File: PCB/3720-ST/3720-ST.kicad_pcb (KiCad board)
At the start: 2 copper layers, 150 x 110 mm, 34 parts, among them J1 1546216-8, J10 1546216-8, J11 1546216-8, J12 1546216-8, J13 1546216-8, J14 1546216-8, J15 1546216-8, J16 1546216-8, J2 1546216-8, J3 1546216-8, J4 1546216-8, J5 1546216-8, J6 1546216-8, J7 1546216-8, J8 1546216-8, J9 1546216-8, U1 TMP275AID, U2 TMP275AID

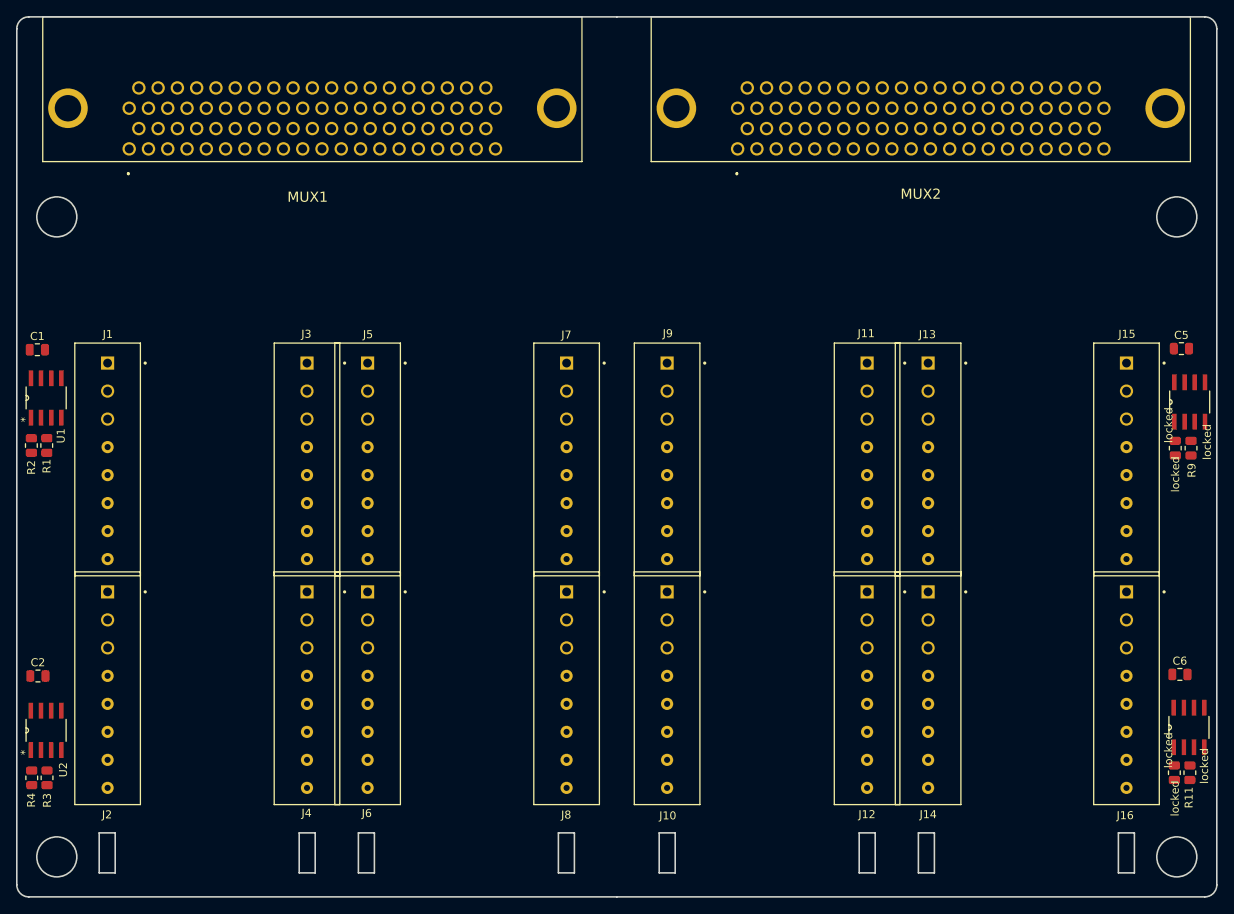
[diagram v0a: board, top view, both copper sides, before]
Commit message: final board layout before routing
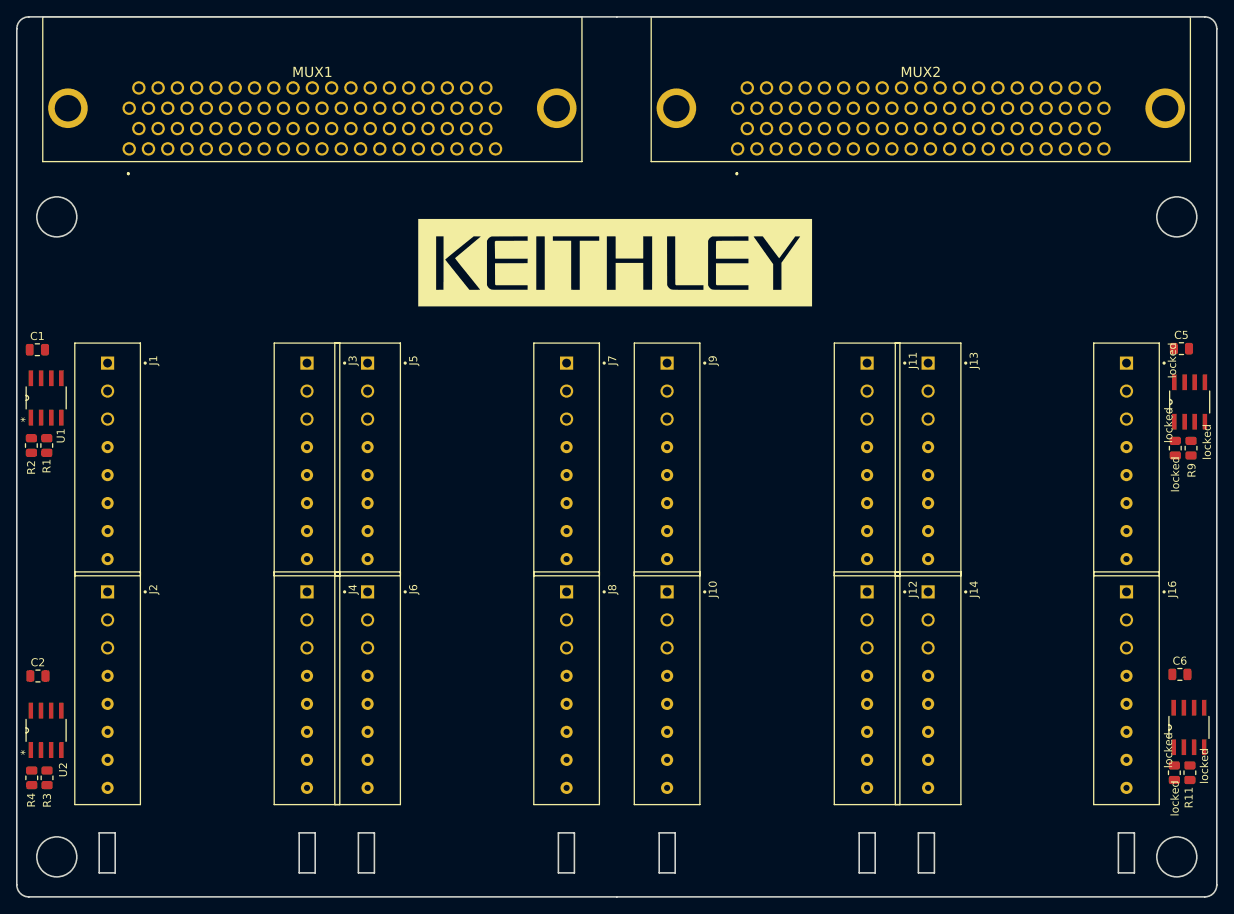
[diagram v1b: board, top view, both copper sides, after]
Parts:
- added G***: LOGO, BVKSound:Keithley_Logo, F.Cu at (99.8, 70.7)
- J1: value 1546216-8 -> locked
- renumbered J15 to locked
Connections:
- MUX1 pad 76: /+ILK -> /ILK1
- MUX1 pad 78: /-ILK -> /ILK1
- MUX2 pad 76: /+ILK -> /ILK2
- MUX2 pad 78: /-ILK -> /ILK2
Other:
- copper layers 2 -> 4

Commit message: Design finished, ready for review
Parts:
- added G***: LOGO, BVKSound:BVKSound_Logo, B.Cu at (156.8, 69.7)
- added QR*****: www.bvksound.be, BVKSound:www.bvksound.be, B.Cu at (138.0, 67.1)
- renumbered locked to J15
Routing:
- net SDA: track 0.00 -> 317.5 mm, vias 0 -> 4
- net +3V3: track 0.00 -> 299.9 mm, vias 0 -> 2
- net GND: track 0.00 -> 284.5 mm, vias 0 -> 153
- net SCL: track 0.00 -> 252.5 mm, vias 0 -> 3
- net /31H: track 0.00 -> 93.6 mm
- net /1H: track 0.00 -> 93.2 mm
- net /31L: track 0.00 -> 91.1 mm
- net /18H: track 0.00 -> 90.5 mm
- net /1L: track 0.00 -> 88.6 mm
- net /2H: track 0.00 -> 88.3 mm
- net /48H: track 0.00 -> 88.0 mm
- net /32H: track 0.00 -> 86.3 mm
- net /18L: track 0.00 -> 86.0 mm
- net /20H: track 0.00 -> 85.6 mm
- net /2L: track 0.00 -> 85.3 mm
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- added copper zone on B.Cu, net GND
- added copper zone on F.Cu, net GND
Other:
- copper layers 4 -> 6
- board text added: "Keithley 3720-ST BVKSound 2022-03"

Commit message: silkscreen added + fix in design
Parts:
- removed QR*****: www.bvksound.be, BVKSound:www.bvksound.be
- added QR1: www.bvksound.be, BVKSound:www.bvksound.be, B.Cu at (136.4, 67.2)
- moved G1 1.17 mm to (156.1, 68.7)
- renumbered G*** to G1
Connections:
- J1 pad 5: /11H -> /11L
- J1 pad 6: /11L -> /11H
- MUX2 pad 40: /39H -> /41H
- MUX2 pad 41: /41H -> /41L
- MUX2 pad 42: /41L -> /33H
- MUX2 pad 43: /33H -> /33L
- MUX2 pad 44: /33L -> /51H
- MUX2 pad 45: /51H -> /51L
- MUX2 pad 46: /51L -> /59H
- MUX2 pad 47: /59H -> /59L
- MUX2 pad 48: /59L -> /40H
- MUX2 pad 49: /40H -> /40L
- MUX2 pad 50: /40L -> /32H
- MUX2 pad 51: /32H -> /32L
- MUX2 pad 52: /32L -> /46L
- MUX2 pad 53: /46L -> unconnected-(MUX2-Pad53)
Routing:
- net GND: track 284.5 -> 114.8 mm, vias 153 -> 194
- net /11H: track 48.8 -> 52.3 mm
- net /11L: track 52.5 -> 49.0 mm
- net /45H: track 36.2 -> 33.9 mm
- net /51H: track 73.6 -> 75.5 mm
- net /51L: track 70.2 -> 71.7 mm
- net /36H: track 68.8 -> 67.4 mm
- net /41H: track 54.3 -> 53.0 mm
- net SCL: track 252.5 -> 253.7 mm
- net /34H: track 78.4 -> 77.3 mm
- net /33H: track 84.9 -> 83.8 mm
- net /43H: track 45.1 -> 44.0 mm
- net /57L: track 46.1 -> 45.0 mm
- net /41L: track 51.8 -> 50.8 mm
- net /32H: track 86.3 -> 87.3 mm
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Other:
- board text added: "15L 15H 13L 13H 11L 11H 9L 9H"
- board text added: "16L 16H 14L 14H 12L 12H 10L 10H"
- board text added: "23L 23H 21L 21H 19L 19H 17L 17H"
- board text added: "24L 24H 22L 22H 20L 20H 18L 18H"
- board text added: "37L 37H 35L 35H 33L 33H 31L 31H"
- board text added: "38L 38H 36L 36H 34L 34H 32L 32H"
- board text added: "45L 45H 43L 43H 41L 41H 39L 39H"
- board text added: "46L 46H 44L 44H 42L 42H 40L 40H"
- board text added: "53L 53H 51L 51H 49L 49H 47L 47H"
- board text added: "54L 54H 52L 52H 50L 50H 48L 48H"
- board text added: "7L 7H 5L 5H 3L 3H 1L 1H"
- board text added: "8L 8H 6L 6H 4L 4H 2L 2H"
- board text added: "MUX_1L MUX_1H 29L 29H 27L 27H 25L 25H"
- board text added: "MUX_2L MUX_2H 59L 59H 57L 57H 55L 55H"
- board text added: "NC NC 30L 30H 28L 28H 26L 26H"
- board text added: "NC NC 60L 60H 58L 58H 56L 56H"

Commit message: latest fixes and added via stitching
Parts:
- added  22: , BVKSound:Via 0.6mm, F.Cu at (75.0, 119.7)
- added  32: , BVKSound:Via 0.6mm, F.Cu at (75.0, 122.2)
- added  33: , BVKSound:Via 0.6mm, F.Cu at (77.5, 122.2)
- added  34: , BVKSound:Via 0.6mm, F.Cu at (47.4, 122.2)
- added  34: , BVKSound:Via 0.6mm, F.Cu at (34.0, 83.2)
- added  34: , BVKSound:Via 0.6mm, F.Cu at (96.1, 83.2)
- added  35: , BVKSound:Via 0.6mm, F.Cu at (34.0, 85.7)
- added  35: , BVKSound:Via 0.6mm, F.Cu at (96.1, 85.7)
- added  36: , BVKSound:Via 0.6mm, F.Cu at (34.0, 88.3)
- added  36: , BVKSound:Via 0.6mm, F.Cu at (96.1, 88.2)
- added  37: , BVKSound:Via 0.6mm, F.Cu at (34.0, 90.8)
- added  37: , BVKSound:Via 0.6mm, F.Cu at (96.1, 90.8)
- added  38: , BVKSound:Via 0.6mm, F.Cu at (34.0, 93.3)
- added  38: , BVKSound:Via 0.6mm, F.Cu at (96.1, 93.3)
- added  39: , BVKSound:Via 0.6mm, F.Cu at (96.1, 95.9)
- added  39: , BVKSound:Via 0.6mm, F.Cu at (34.0, 95.9)
- added  40: , BVKSound:Via 0.6mm, F.Cu at (34.0, 98.4)
- added  40: , BVKSound:Via 0.6mm, F.Cu at (96.1, 98.4)
- added  41: , BVKSound:Via 0.6mm, F.Cu at (96.1, 100.9)
- added  41: , BVKSound:Via 0.6mm, F.Cu at (34.0, 101.0)
- added  42: , BVKSound:Via 0.6mm, F.Cu at (75.0, 124.8)
- added  43: , BVKSound:Via 0.6mm, F.Cu at (77.5, 124.8)
- added  44: , BVKSound:Via 0.6mm, F.Cu at (47.4, 124.8)
- added  44: , BVKSound:Via 0.6mm, F.Cu at (80.0, 124.8)
- added  45: , BVKSound:Via 0.6mm, F.Cu at (34.0, 103.5)
- added  45: , BVKSound:Via 0.6mm, F.Cu at (96.1, 103.5)
- added  46: , BVKSound:Via 0.6mm, F.Cu at (34.0, 106.0)
- added  46: , BVKSound:Via 0.6mm, F.Cu at (96.1, 106.0)
- added  47: , BVKSound:Via 0.6mm, F.Cu at (96.1, 108.6)
- added  47: , BVKSound:Via 0.6mm, F.Cu at (34.0, 108.6)
- added  48: , BVKSound:Via 0.6mm, F.Cu at (34.0, 111.1)
- added  48: , BVKSound:Via 0.6mm, F.Cu at (96.1, 111.1)
- added  49: , BVKSound:Via 0.6mm, F.Cu at (34.0, 113.7)
- added  49: , BVKSound:Via 0.6mm, F.Cu at (96.1, 113.6)
- added  50: , BVKSound:Via 0.6mm, F.Cu at (34.0, 116.2)
- added  50: , BVKSound:Via 0.6mm, F.Cu at (96.1, 116.2)
- added  51: , BVKSound:Via 0.6mm, F.Cu at (96.1, 118.7)
- added  51: , BVKSound:Via 0.6mm, F.Cu at (34.0, 118.7)
- added  52: , BVKSound:Via 0.6mm, F.Cu at (75.0, 127.3)
- added  53: , BVKSound:Via 0.6mm, F.Cu at (77.5, 127.3)
- added  53: , BVKSound:Via 0.6mm, F.Cu at (44.9, 127.3)
- added  54: , BVKSound:Via 0.6mm, F.Cu at (80.0, 127.3)
- added  54: , BVKSound:Via 0.6mm, F.Cu at (47.4, 127.3)
- added  55: , BVKSound:Via 0.6mm, F.Cu at (49.9, 127.3)
- added  55: , BVKSound:Via 0.6mm, F.Cu at (82.6, 127.3)
- added  56: , BVKSound:Via 0.6mm, F.Cu at (96.1, 121.3)
- added  56: , BVKSound:Via 0.6mm, F.Cu at (34.0, 121.3)
- added  57: , BVKSound:Via 0.6mm, F.Cu at (96.1, 123.8)
- added  57: , BVKSound:Via 0.6mm, F.Cu at (34.0, 123.8)
- added  58: , BVKSound:Via 0.6mm, F.Cu at (96.1, 126.3)
- added  58: , BVKSound:Via 0.6mm, F.Cu at (34.0, 126.4)
- added  59: , BVKSound:Via 0.6mm, F.Cu at (96.1, 128.9)
- added  59: , BVKSound:Via 0.6mm, F.Cu at (34.0, 128.9)
- added  60: , BVKSound:Via 0.6mm, F.Cu at (96.1, 131.4)
- added  60: , BVKSound:Via 0.6mm, F.Cu at (34.0, 131.4)
- added  61: , BVKSound:Via 0.6mm, F.Cu at (34.0, 134.0)
- added  61: , BVKSound:Via 0.6mm, F.Cu at (96.1, 134.0)
- added  62: , BVKSound:Via 0.6mm, F.Cu at (75.0, 129.9)
- added  62: , BVKSound:Via 0.6mm, F.Cu at (42.3, 129.8)
- added  63: , BVKSound:Via 0.6mm, F.Cu at (77.5, 129.9)
- added  63: , BVKSound:Via 0.6mm, F.Cu at (44.9, 129.8)
- added  64: , BVKSound:Via 0.6mm, F.Cu at (80.0, 129.9)
- added  64: , BVKSound:Via 0.6mm, F.Cu at (47.4, 129.8)
- added  65: , BVKSound:Via 0.6mm, F.Cu at (82.6, 129.9)
- added  65: , BVKSound:Via 0.6mm, F.Cu at (49.9, 129.8)
- added  66: , BVKSound:Via 0.6mm, F.Cu at (85.1, 129.9)
- added  66: , BVKSound:Via 0.6mm, F.Cu at (52.5, 129.8)
- added  67: , BVKSound:Via 0.6mm, F.Cu at (96.1, 136.5)
- added  67: , BVKSound:Via 0.6mm, F.Cu at (34.0, 136.5)
- added  72: , BVKSound:Via 0.6mm, F.Cu at (42.3, 132.4)
- added  72: , BVKSound:Via 0.6mm, F.Cu at (75.0, 132.4)
- added  73: , BVKSound:Via 0.6mm, F.Cu at (77.5, 132.4)
- added  73: , BVKSound:Via 0.6mm, F.Cu at (44.9, 132.4)
- added  74: , BVKSound:Via 0.6mm, F.Cu at (47.4, 132.4)
- added  74: , BVKSound:Via 0.6mm, F.Cu at (80.0, 132.4)
- added  75: , BVKSound:Via 0.6mm, F.Cu at (82.6, 132.4)
- added  75: , BVKSound:Via 0.6mm, F.Cu at (49.9, 132.4)
- added  76: , BVKSound:Via 0.6mm, F.Cu at (52.5, 132.4)
- added  76: , BVKSound:Via 0.6mm, F.Cu at (85.1, 132.4)
- added  77: , BVKSound:Via 0.6mm, F.Cu at (87.7, 132.4)
- added  77: , BVKSound:Via 0.6mm, F.Cu at (55.0, 132.4)
- added  82: , BVKSound:Via 0.6mm, F.Cu at (42.3, 134.9)
- added  82: , BVKSound:Via 0.6mm, F.Cu at (75.0, 134.9)
- added  83: , BVKSound:Via 0.6mm, F.Cu at (77.5, 134.9)
- added  83: , BVKSound:Via 0.6mm, F.Cu at (44.9, 134.9)
- added  84: , BVKSound:Via 0.6mm, F.Cu at (80.0, 134.9)
- added  84: , BVKSound:Via 0.6mm, F.Cu at (47.4, 134.9)
- added  85: , BVKSound:Via 0.6mm, F.Cu at (49.9, 134.9)
- added  85: , BVKSound:Via 0.6mm, F.Cu at (82.6, 134.9)
- added  86: , BVKSound:Via 0.6mm, F.Cu at (85.1, 134.9)
- added  86: , BVKSound:Via 0.6mm, F.Cu at (52.5, 134.9)
- added  87: , BVKSound:Via 0.6mm, F.Cu at (55.0, 134.9)
- added  87: , BVKSound:Via 0.6mm, F.Cu at (87.7, 134.9)
- added  92: , BVKSound:Via 0.6mm, F.Cu at (75.0, 137.5)
- added  92: , BVKSound:Via 0.6mm, F.Cu at (42.3, 137.4)
- added  93: , BVKSound:Via 0.6mm, F.Cu at (77.5, 137.5)
- added  93: , BVKSound:Via 0.6mm, F.Cu at (44.9, 137.4)
- added  94: , BVKSound:Via 0.6mm, F.Cu at (47.4, 137.4)
- added  94: , BVKSound:Via 0.6mm, F.Cu at (80.0, 137.5)
- added  95: , BVKSound:Via 0.6mm, F.Cu at (82.6, 137.5)
- added  95: , BVKSound:Via 0.6mm, F.Cu at (49.9, 137.4)
- added  96: , BVKSound:Via 0.6mm, F.Cu at (85.1, 137.5)
- added  96: , BVKSound:Via 0.6mm, F.Cu at (52.5, 137.4)
- added  97: , BVKSound:Via 0.6mm, F.Cu at (87.7, 137.5)
- added  97: , BVKSound:Via 0.6mm, F.Cu at (55.0, 137.4)
- added 1: , , F.Cu at (104.2, 85.7)
- added 1: , , F.Cu at (165.8, 85.5)
- added 10: , , F.Cu at (104.2, 106.0)
- added 10: , , F.Cu at (165.8, 105.8)
- added 11: , , F.Cu at (104.2, 108.6)
- added 11: , , F.Cu at (165.8, 108.3)
- added 12: , , F.Cu at (104.2, 111.1)
- added 12: , , F.Cu at (165.8, 110.9)
- added 13: , , F.Cu at (104.2, 113.7)
- added 13: , , F.Cu at (165.8, 113.4)
- added 14: , , F.Cu at (104.2, 116.2)
- added 14: , , F.Cu at (165.8, 116.0)
- added 15: , , F.Cu at (122.3, 117.2)
- added 16: , , F.Cu at (165.8, 118.5)
- added 16: , , F.Cu at (104.2, 118.8)
- added 17: , , F.Cu at (104.2, 121.3)
- added 17: , , F.Cu at (165.8, 121.0)
- added 18: , , F.Cu at (165.8, 123.6)
- added 18: , , F.Cu at (104.2, 123.8)
- added 19: , , F.Cu at (165.8, 126.1)
- added 19: , , F.Cu at (104.2, 126.4)
- added 2: , , F.Cu at (104.2, 88.3)
- added 2: , , F.Cu at (165.8, 88.0)
- added 20: , , F.Cu at (104.2, 128.9)
- added 20: , , F.Cu at (165.8, 128.7)
- added 21: , , F.Cu at (165.8, 131.2)
- added 21: , , F.Cu at (104.2, 131.4)
- added 22: , , F.Cu at (165.8, 133.7)
- added 22: , , F.Cu at (104.2, 134.0)
- added 23: , , F.Cu at (104.2, 136.5)
- added 23: , , F.Cu at (165.8, 136.3)
- added 25: , , F.Cu at (122.3, 119.7)
- added 3: , , F.Cu at (104.2, 90.8)
- added 3: , , F.Cu at (165.8, 90.6)
- added 33: , , F.Cu at (145.6, 122.2)
- added 34: , , F.Cu at (119.8, 122.2)
- added 35: , , F.Cu at (122.3, 122.2)
- added 4: , , F.Cu at (104.2, 93.3)
- added 4: , , F.Cu at (165.8, 93.1)
- added 43: , , F.Cu at (145.6, 124.8)
- added 44: , , F.Cu at (119.8, 124.8)
- added 44: , , F.Cu at (148.1, 124.8)
- added 45: , , F.Cu at (122.3, 124.8)
- added 5: , , F.Cu at (122.3, 114.6)
- added 53: , , F.Cu at (145.6, 127.3)
- added 53: , , F.Cu at (117.2, 127.3)
- added 54: , , F.Cu at (119.8, 127.3)
- added 54: , , F.Cu at (148.1, 127.3)
- added 55: , , F.Cu at (150.7, 127.3)
- added 55: , , F.Cu at (122.3, 127.3)
- added 6: , , F.Cu at (104.2, 95.9)
- added 6: , , F.Cu at (165.8, 95.6)
- added 62: , , F.Cu at (114.7, 129.9)
- added 63: , , F.Cu at (145.6, 129.9)
- added 63: , , F.Cu at (117.2, 129.9)
- added 64: , , F.Cu at (148.1, 129.9)
- added 64: , , F.Cu at (119.8, 129.9)
- added 65: , , F.Cu at (150.7, 129.9)
- added 65: , , F.Cu at (122.3, 129.9)
- added 66: , , F.Cu at (153.2, 129.9)
- added 7: , , F.Cu at (165.8, 98.2)
- added 7: , , F.Cu at (104.2, 98.4)
- added 71: , , F.Cu at (112.1, 132.4)
- added 72: , , F.Cu at (114.7, 132.4)
- added 73: , , F.Cu at (117.2, 132.4)
- added 73: , , F.Cu at (145.6, 132.4)
- added 74: , , F.Cu at (119.8, 132.4)
- added 74: , , F.Cu at (148.1, 132.4)
- added 75: , , F.Cu at (150.7, 132.4)
- added 75: , , F.Cu at (122.3, 132.4)
- added 76: , , F.Cu at (124.8, 132.4)
- added 76: , , F.Cu at (153.2, 132.4)
- added 77: , , F.Cu at (155.8, 132.4)
- added 8: , , F.Cu at (165.8, 100.7)
- added 8: , , F.Cu at (104.2, 101.0)
- added 81: , , F.Cu at (112.1, 134.9)
- added 82: , , F.Cu at (114.7, 134.9)
- added 83: , , F.Cu at (117.2, 134.9)
- added 83: , , F.Cu at (145.6, 134.9)
- added 84: , , F.Cu at (119.8, 134.9)
- added 84: , , F.Cu at (148.1, 134.9)
- added 85: , , F.Cu at (122.3, 134.9)
- added 85: , , F.Cu at (150.7, 134.9)
- added 86: , , F.Cu at (153.2, 134.9)
- added 86: , , F.Cu at (124.8, 134.9)
- added 87: , , F.Cu at (155.8, 134.9)
- added 88: , , F.Cu at (158.3, 134.9)
- added 9: , , F.Cu at (165.8, 103.3)
- added 9: , , F.Cu at (104.2, 103.5)
- added 91: , , F.Cu at (112.1, 137.5)
- added 92: , , F.Cu at (114.7, 137.5)
- added 93: , , F.Cu at (117.2, 137.5)
- added 93: , , F.Cu at (145.6, 137.5)
- added 94: , , F.Cu at (148.1, 137.5)
- added 94: , , F.Cu at (119.8, 137.5)
- added 95: , , F.Cu at (150.7, 137.5)
- added 95: , , F.Cu at (122.3, 137.5)
- added 96: , , F.Cu at (124.8, 137.5)
- added 96: , , F.Cu at (153.2, 137.5)
- added 97: , , F.Cu at (155.8, 137.5)
- added 98: , , F.Cu at (158.3, 137.5)
- added ?: , , F.Cu at (165.8, 82.9)
- added ?: , , F.Cu at (104.2, 83.2)
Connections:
- MUX2 pad 73: /3V3 -> +3V3
- MUX2 pad 74: /SCLK -> SCL
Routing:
- net GND: track 114.8 -> 287.9 mm, vias 194 -> 2
- net SCL: track 253.7 -> 327.4 mm, vias 3 -> 4
- net +3V3: track 299.9 -> 361.8 mm, vias 2 -> 3
- net SDA: track 317.5 -> 321.0 mm
- added copper zone on B.Cu, net Shield1
- added copper zone on F.Cu, net Shield1
- added copper zone on B.Cu, net Shield2
- added copper zone on F.Cu, net Shield2
- removed copper zone on B.Cu, net GND
- removed copper zone on F.Cu, net GND

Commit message: final rev before manufacturing
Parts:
- removed the  48 at (34.0, 111.1)
- removed the  49 at (34.0, 113.7)
- removed the  50 at (34.0, 116.2)
- removed the  51 at (34.0, 118.7)
- removed the  56 at (34.0, 121.3)
- removed the  57 at (34.0, 123.8)
- removed the  58 at (34.0, 126.4)
- removed the  59 at (34.0, 128.9)
- removed the  60 at (34.0, 131.4)
- removed the  61 at (34.0, 134.0)
- removed the  67 at (34.0, 136.5)
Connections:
-  34 pad 1: (no net) -> Shield1 (x2)
-  35 pad 1: (no net) -> Shield1 (x2)
-  36 pad 1: (no net) -> Shield1 (x2)
-  37 pad 1: (no net) -> Shield1 (x2)
-  38 pad 1: (no net) -> Shield1 (x2)
-  39 pad 1: (no net) -> Shield1 (x2)
-  40 pad 1: (no net) -> Shield1 (x2)
-  41 pad 1: (no net) -> Shield1 (x2)
-  45 pad 1: (no net) -> Shield1 (x2)
-  46 pad 1: (no net) -> Shield1
-  47 pad 1: (no net) -> Shield1 (x2)
-  48 pad 1: (no net) -> Shield1
-  49 pad 1: (no net) -> Shield1
-  50 pad 1: (no net) -> Shield1
-  51 pad 1: (no net) -> Shield1
-  56 pad 1: (no net) -> Shield1
-  57 pad 1: (no net) -> Shield1
-  58 pad 1: (no net) -> Shield1
-  59 pad 1: (no net) -> Shield1
-  60 pad 1: (no net) -> Shield1
-  61 pad 1: (no net) -> Shield1
-  67 pad 1: (no net) -> Shield1
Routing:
- net /1H: track 93.2 -> 97.1 mm
- net /4L: track 74.5 -> 77.8 mm
- net /6L: track 63.7 -> 64.9 mm
- net /16H: track 39.8 -> 40.3 mm

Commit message: Update after rev1 Board
Screw terminal package update due to error in hole sizes. Overall board height reduced by 2mm.
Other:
- board size 150 x 110 mm -> 150 x 108 mm
- board text added: "Keithley 3720-ST BVKSound 2022-04 Rev.2"
- board text removed: "Keithley 3720-ST BVKSound 2022-03"
